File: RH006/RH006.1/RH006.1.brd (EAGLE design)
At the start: 49.5 x 49.5 mm, 40 parts, among them CN1 USB, CN4 FTDI, Q2 BSS138, Q3 BSS138, U1 ATMega-328, U3 MCP1703CB, X1 16 MHz

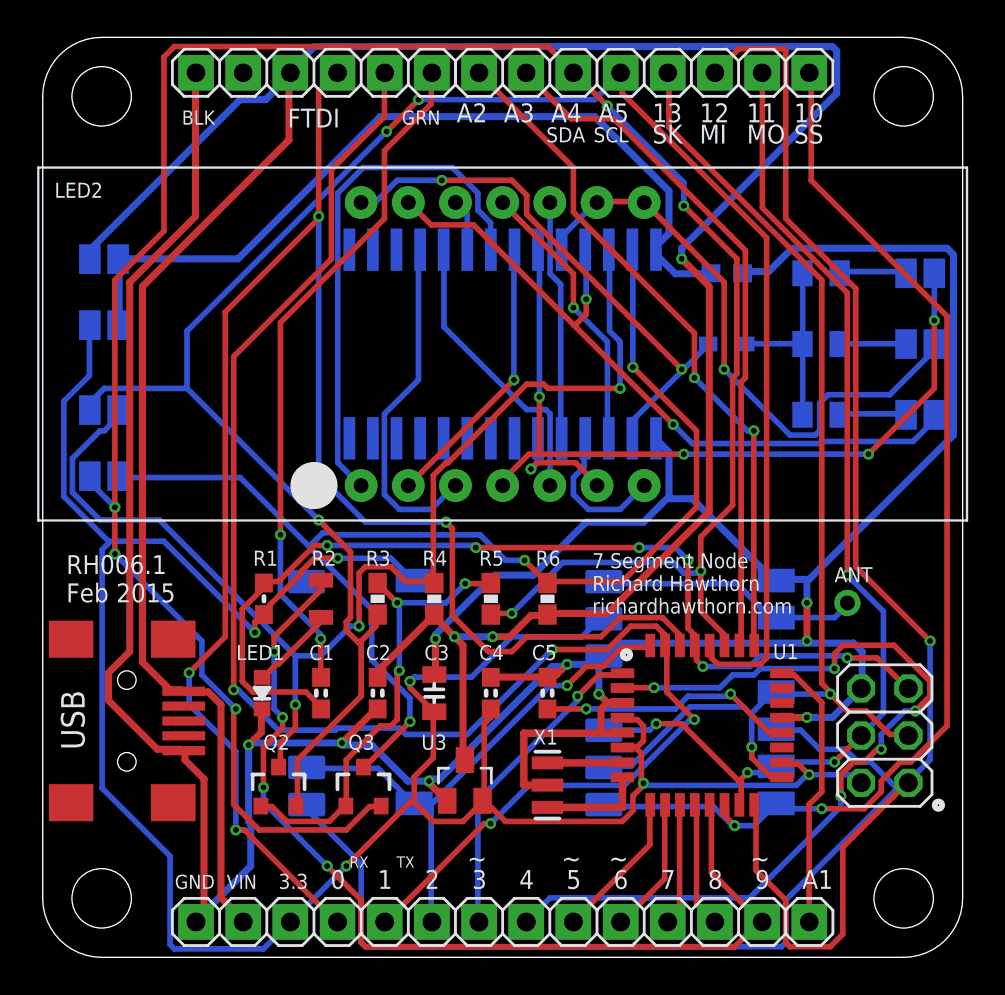
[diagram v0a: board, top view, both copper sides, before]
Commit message: Prepare board 6 for production, version 1 finished
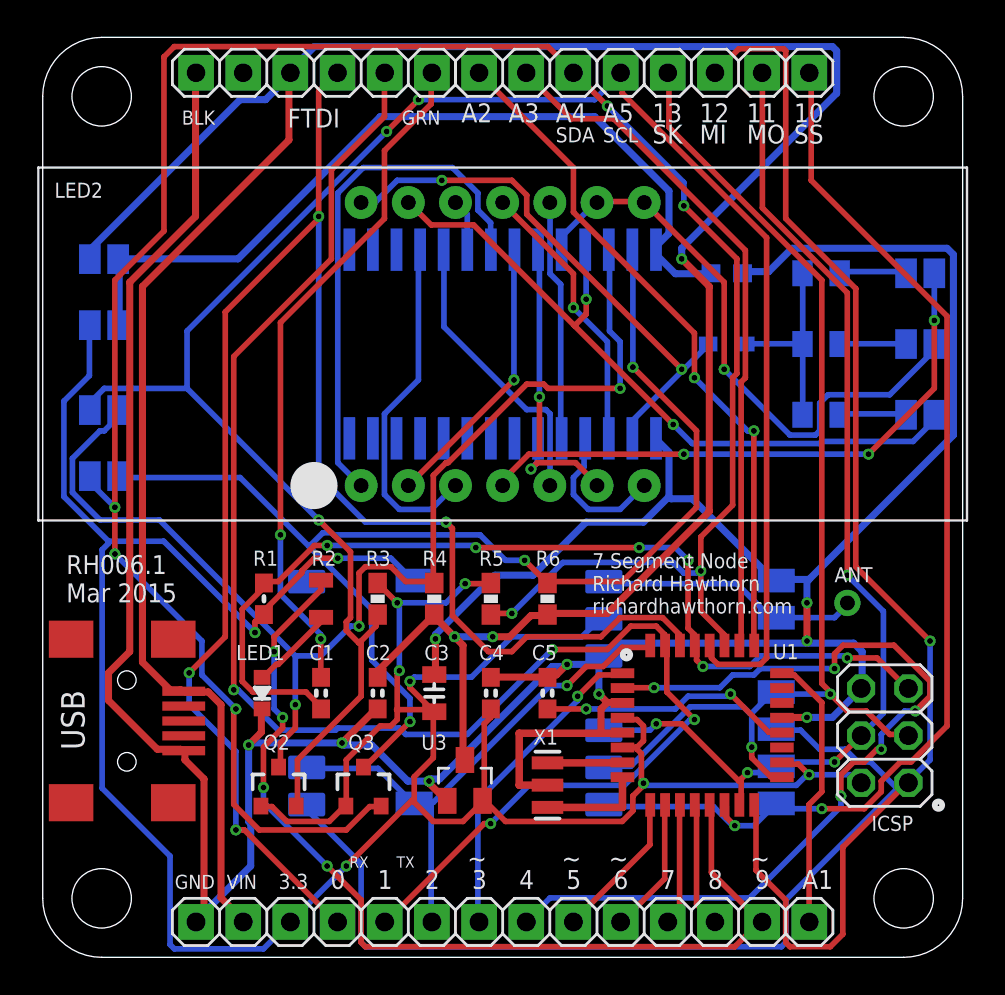
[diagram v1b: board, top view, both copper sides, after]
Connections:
- removed net VCC: Q2.1, Q3.1, R3.1, R5.1
- net 3.3V: now also Q2.1, Q3.1, R3.1, R5.1
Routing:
- net 3.3V: track 133.4 -> 160.6 mm, vias 6 -> 9
- net VCC: track 24.8 -> 0.00 mm, vias 3 -> 0
- net GND: track 198.3 -> 198.8 mm
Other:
- board text added: "3.3v"
- board text added: "3.3v i2c"
- board text added: "5v"
- board text added: "LED Power"
- board text added: "RH006.1 Mar 2015"
- board text removed: "3.3V"
- board text removed: "5V"
- board text removed: "5V I2C"
- board text removed: "RH006.1 Feb 2015"
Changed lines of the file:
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@@
 <wire x1="49.53" y1="46.355" x2="49.53" y2="3.175" width="0.0254" layer="20"/>
 <text x="1.27" y="19.1135" size="1.016" layer="25">RH006.1
-Feb 2015</text>
+Mar 2015</text>
 <text x="29.591" y="18.51025" size="0.8128" layer="25">7 Segment Node
 Richard Hawthorn
@@
 <text x="35.3695" y="43.815" size="1.016" layer="25">MI</text>
 <text x="32.8295" y="43.815" size="1.016" layer="25">SK</text>
-<text x="29.9085" y="44.958" size="1.016" layer="25">A5</text>
-<text x="27.3685" y="44.958" size="1.016" layer="25">A4</text>
-<text x="24.8285" y="44.958" size="1.016" layer="25">A3</text>
-<text x="22.2885" y="44.958" size="1.016" layer="25">A2</text>
-<text x="29.6545" y="43.8785" size="0.8128" layer="25">SCL</text>
-<text x="27.1145" y="43.8785" size="0.8128" layer="25">SDA</text>
+<text x="30.1625" y="44.958" size="1.016" layer="25">A5</text>
+<text x="27.6225" y="44.958" size="1.016" layer="25">A4</text>
+<text x="25.0825" y="44.958" size="1.016" layer="25">A3</text>
+<text x="22.5425" y="44.958" size="1.016" layer="25">A2</text>
+<text x="30.1625" y="43.8785" size="0.8128" layer="25">SCL</text>
+<text x="27.6225" y="43.8785" size="0.8128" layer="25">SDA</text>
 <text x="9.906" y="3.683" size="0.762" layer="25">VIN</text>
 <text x="12.7" y="3.683" size="0.8128" layer="25">3.3</text>
@@
 <text x="40.894" y="3.683" size="1.016" layer="25">A1</text>
 <text x="7.112" y="3.683" size="0.762" layer="25">GND</text>
-<text x="7.874" y="37.084" size="1.27" layer="26" rot="MR0">5V</text>
-<text x="9.398" y="33.528" size="1.27" layer="26" rot="MR0">3.3V</text>
-<text x="11.176" y="27.178" size="1.27" layer="26" rot="MR0">5V I2C</text>
+<text x="7.62" y="37.084" size="1.27" layer="26" rot="MR0">5v</text>
+<text x="9.398" y="33.528" size="1.27" layer="26" rot="MR0">3.3v</text>
+<text x="13.716" y="27.178" size="1.27" layer="26" rot="MR0">3.3v i2c</text>
+<text x="11.684" y="40.132" size="0.8128" layer="26" rot="MR0">LED Power</text>
 </plain>
 <attributes>
@@
 <description language="de">&lt;b&gt;EAGLE Design Rules&lt;/b&gt;
 &lt;p&gt;
-Die Standard-Design-Rules sind so gewÃÂÃÂÃÂÃÂÃÂÃÂÃÂÃÂ¤hlt, dass sie fÃÂÃÂÃÂÃÂÃÂÃÂÃÂÃÂ¼r
+Die Standard-Design-Rules sind so gewÃÂÃÂÃÂÃÂÃÂÃÂÃÂÃÂÃÂÃÂÃÂÃÂÃÂÃÂÃÂÃÂ¤hlt, dass sie fÃÂÃÂÃÂÃÂÃÂÃÂÃÂÃÂÃÂÃÂÃÂÃÂÃÂÃÂÃÂÃÂ¼r
 die meisten Anwendungen passen. Sollte ihre Platine
 besondere Anforderungen haben, treffen Sie die erforderlichen
@@
 <param name="TopRouterVariant" value="1"/>
 <param name="tpViaShape" value="round"/>
-<param name="PrefDir.1" value="a"/>
+<param name="PrefDir.1" value="*"/>
 <param name="PrefDir.2" value="0"/>
 <param name="PrefDir.3" value="0"/>
@@
 <param name="PrefDir.14" value="0"/>
 <param name="PrefDir.15" value="0"/>
-<param name="PrefDir.16" value="a"/>
+<param name="PrefDir.16" value="-"/>
 <param name="cfVia" value="8"/>
 <param name="cfNonPref" value="5"/>
@@
 <element name="CN4" library="pinhead" package="1X06" value="FTDI" x="14.605" y="47.625" smashed="yes"/>
 <element name="ICSP1" library="pinhead" package="2X03" value="ICSP" x="45.339" y="11.938" smashed="yes" rot="R90">
-<attribute name="VALUE" x="46.863" y="7.62" size="0.8128" layer="27" rot="R180"/>
+<attribute name="VALUE" x="46.863" y="7.62" size="0.8128" layer="25" rot="R180"/>
 </element>
 <element name="JP3" library="pinhead" package="1X14" value="" x="24.765" y="1.905" smashed="yes" rot="R180">
@@
 <contactref element="U4" pad="P$1"/>
 <contactref element="C6" pad="2"/>
-<wire x1="27.178" y1="9.271" x2="25.908" y2="9.271" width="0.4064" layer="1"/>
-<wire x1="25.908" y1="9.271" x2="25.908" y2="12.065" width="0.4064" layer="1"/>
-<wire x1="25.908" y1="12.065" x2="30.0609" y2="12.065" width="0.4064" layer="1"/>
+<wire x1="27.178" y1="9.271" x2="25.654" y2="9.271" width="0.4064" layer="1"/>
+<wire x1="25.654" y1="9.271" x2="25.654" y2="12.065" width="0.4064" layer="1"/>
+<wire x1="25.654" y1="12.065" x2="30.0609" y2="12.065" width="0.4064" layer="1"/>
 <wire x1="30.0609" y1="12.065" x2="31.2166" y2="12.065" width="0.4064" layer="1"/>
 <wire x1="31.2166" y1="12.065" x2="31.2166" y2="12.0968" width="0.4064" layer="1"/>
@@
 <wire x1="19.7739" y1="14.859" x2="20.0025" y2="15.0876" width="0.3048" layer="16"/>
 <wire x1="19.7739" y1="14.5161" x2="19.7739" y2="14.859" width="0.3048" layer="1"/>
-<wire x1="21.0312" y1="13.2588" x2="19.7739" y2="14.5161" width="0.3048" layer="1"/>
+<wire x1="21.0312" y1="13.2588" x2="20.955" y2="13.335" width="0.3048" layer="1"/>
+<wire x1="20.955" y1="13.335" x2="19.7739" y2="14.5161" width="0.3048" layer="1"/>
 <wire x1="30.1752" y1="18.1737" x2="30.2123" y2="18.224" width="0.3048" layer="16"/>
 <wire x1="21.0312" y1="13.2588" x2="21.082" y2="13.224" width="0.3048" layer="1"/>
@@
 <via x="16.3449" y="4.9149" extent="1-16" drill="0.3048"/>
 <via x="32.3469" y="9.3726" extent="1-16" drill="0.3048"/>
+<contactref element="R3" pad="1"/>
+<contactref element="Q2" pad="1"/>
+<contactref element="Q3" pad="1"/>
+<contactref element="R5" pad="1"/>
+<wire x1="12.3444" y1="8.1153" x2="11.7729" y2="8.1153" width="0.3048" layer="1"/>
+<wire x1="13.1445" y1="7.3152" x2="12.3444" y2="8.1153" width="0.3048" layer="1"/>
+<wire x1="15.4305" y1="7.3152" x2="13.1445" y2="7.3152" width="0.3048" layer="1"/>
+<wire x1="16.2306" y1="8.1153" x2="15.4305" y2="7.3152" width="0.3048" layer="1"/>
+<wire x1="16.2306" y1="8.1153" x2="16.322" y2="8.144" width="0.3048" layer="1"/>
+<wire x1="19.0881" y1="19.0881" x2="18.1356" y2="20.0406" width="0.3048" layer="1"/>
+<wire x1="18.1356" y1="20.0406" x2="18.0594" y2="20.1168" width="0.3048" layer="1"/>
+<wire x1="21.717" y1="19.0881" x2="19.0881" y2="19.0881" width="0.3048" layer="16"/>
+<wire x1="22.7457" y1="20.1168" x2="21.717" y2="19.0881" width="0.3048" layer="16"/>
+<wire x1="24.1173" y1="20.1168" x2="22.7457" y2="20.1168" width="0.3048" layer="1"/>
+<wire x1="24.1173" y1="20.1168" x2="24.13" y2="20.154" width="0.3048" layer="1"/>
+<wire x1="16.3449" y1="10.6299" x2="16.3449" y2="8.2296" width="0.3048" layer="1"/>
+<wire x1="18.1737" y1="12.4587" x2="16.3449" y2="10.6299" width="0.3048" layer="1"/>
+<wire x1="18.7452" y1="12.4587" x2="18.1737" y2="12.4587" width="0.3048" layer="1"/>
+<wire x1="19.0881" y1="12.8016" x2="18.7452" y2="12.4587" width="0.3048" layer="1"/>
+<wire x1="19.0881" y1="15.3162" x2="19.0881" y2="13.335" width="0.3048" layer="1"/>
+<wire x1="19.0881" y1="13.335" x2="19.0881" y2="12.8016" width="0.3048" layer="1"/>
+<wire x1="19.2024" y1="15.4305" x2="19.0881" y2="15.3162" width="0.3048" layer="1"/>
+<wire x1="19.2024" y1="18.9738" x2="19.2024" y2="15.4305" width="0.3048" layer="16"/>
+<wire x1="16.3449" y1="8.2296" x2="16.322" y2="8.144" width="0.3048" layer="1"/>
+<wire x1="19.2024" y1="18.9738" x2="19.0881" y2="19.0881" width="0.3048" layer="16"/>
+<via x="19.0881" y="19.0881" extent="1-16" drill="0.3048"/>
+<via x="22.7457" y="20.1168" extent="1-16" drill="0.3048"/>
+<via x="19.2024" y="15.4305" extent="1-16" drill="0.3048"/>
+<wire x1="11.7475" y1="8.255" x2="11.75" y2="8.144" width="0.3048" layer="1"/>
+<wire x1="11.7475" y1="8.255" x2="11.7729" y2="8.1153" width="0.3048" layer="1"/>
+<wire x1="18.0975" y1="20.0025" x2="18.1356" y2="20.0406" width="0.3048" layer="1"/>
+<wire x1="18.0975" y1="20.0025" x2="18.034" y2="20.154" width="0.3048" layer="1"/>
+<wire x1="20.955" y1="13.335" x2="19.0881" y2="13.335" width="0.3048" layer="1"/>
+<wire x1="19.05" y1="13.335" x2="19.0881" y2="13.335" width="0.3048" layer="1"/>
+<wire x1="20.955" y1="13.335" x2="21.082" y2="13.224" width="0.3048" layer="1"/>
 </signal>
 <signal name="N$19">
@@
 <via x="31.7754" y="31.7754" extent="1-16" drill="0.3048"/>
 </signal>
-<signal name="VCC">
-<contactref element="Q2" pad="1"/>
-<contactref element="R3" pad="1"/>
-<contactref element="Q3" pad="1"/>
-<contactref element="R5" pad="1"/>
-<wire x1="12.3444" y1="8.1153" x2="11.7729" y2="8.1153" width="0.3048" layer="1"/>
-<wire x1="13.1445" y1="7.3152" x2="12.3444" y2="8.1153" width="0.3048" layer="1"/>
-<wire x1="15.4305" y1="7.3152" x2="13.1445" y2="7.3152" width="0.3048" layer="1"/>
-<wire x1="16.2306" y1="8.1153" x2="15.4305" y2="7.3152" width="0.3048" layer="1"/>
-<wire x1="11.7729" y1="8.1153" x2="11.75" y2="8.144" width="0.3048" layer="1"/>
-<wire x1="16.2306" y1="8.1153" x2="16.322" y2="8.144" width="0.3048" layer="1"/>
-<wire x1="19.0881" y1="19.0881" x2="18.0594" y2="20.1168" width="0.3048" layer="1"/>
-<wire x1="21.717" y1="19.0881" x2="19.0881" y2="19.0881" width="0.3048" layer="16"/>
-<wire x1="22.7457" y1="20.1168" x2="21.717" y2="19.0881" width="0.3048" layer="16"/>
-<wire x1="24.1173" y1="20.1168" x2="22.7457" y2="20.1168" width="0.3048" layer="1"/>
-<wire x1="18.0594" y1="20.1168" x2="18.034" y2="20.154" width="0.3048" layer="1"/>
-<wire x1="24.1173" y1="20.1168" x2="24.13" y2="20.154" width="0.3048" layer="1"/>
-<wire x1="16.3449" y1="10.6299" x2="16.3449" y2="8.2296" width="0.3048" layer="1"/>
-<wire x1="18.1737" y1="12.4587" x2="16.3449" y2="10.6299" width="0.3048" layer="1"/>
-<wire x1="18.7452" y1="12.4587" x2="18.1737" y2="12.4587" width="0.3048" layer="1"/>
-<wire x1="19.0881" y1="12.8016" x2="18.7452" y2="12.4587" width="0.3048" layer="1"/>
-<wire x1="19.0881" y1="15.3162" x2="19.0881" y2="12.8016" width="0.3048" layer="1"/>
-<wire x1="19.2024" y1="15.4305" x2="19.0881" y2="15.3162" width="0.3048" layer="1"/>
-<wire x1="19.2024" y1="18.9738" x2="19.2024" y2="15.4305" width="0.3048" layer="16"/>
-<wire x1="16.3449" y1="8.2296" x2="16.322" y2="8.144" width="0.3048" layer="1"/>
-<wire x1="19.2024" y1="18.9738" x2="19.0881" y2="19.0881" width="0.3048" layer="16"/>
-<via x="19.0881" y="19.0881" extent="1-16" drill="0.3048"/>
-<via x="22.7457" y="20.1168" extent="1-16" drill="0.3048"/>
-<via x="19.2024" y="15.4305" extent="1-16" drill="0.3048"/>
-</signal>
 <signal name="VLED" class="1">
